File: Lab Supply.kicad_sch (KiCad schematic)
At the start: 38 parts, among them J1 V+, J2 V-, Q1 TIP121, Q2 2N2222, T1 115V to 24V, U1 LM358, U2 LM358

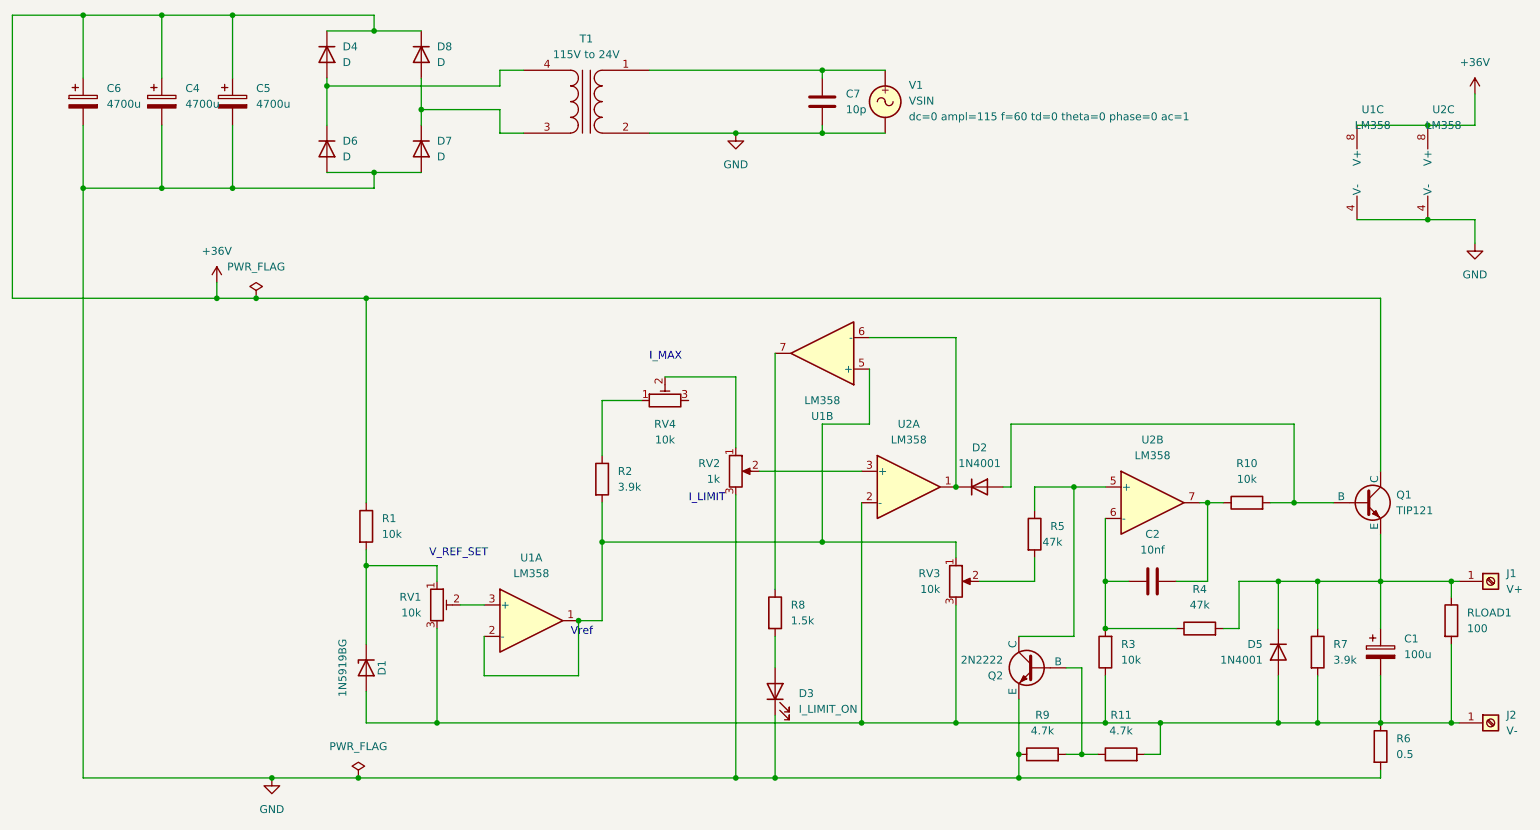
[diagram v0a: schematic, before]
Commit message: Changed to LM324
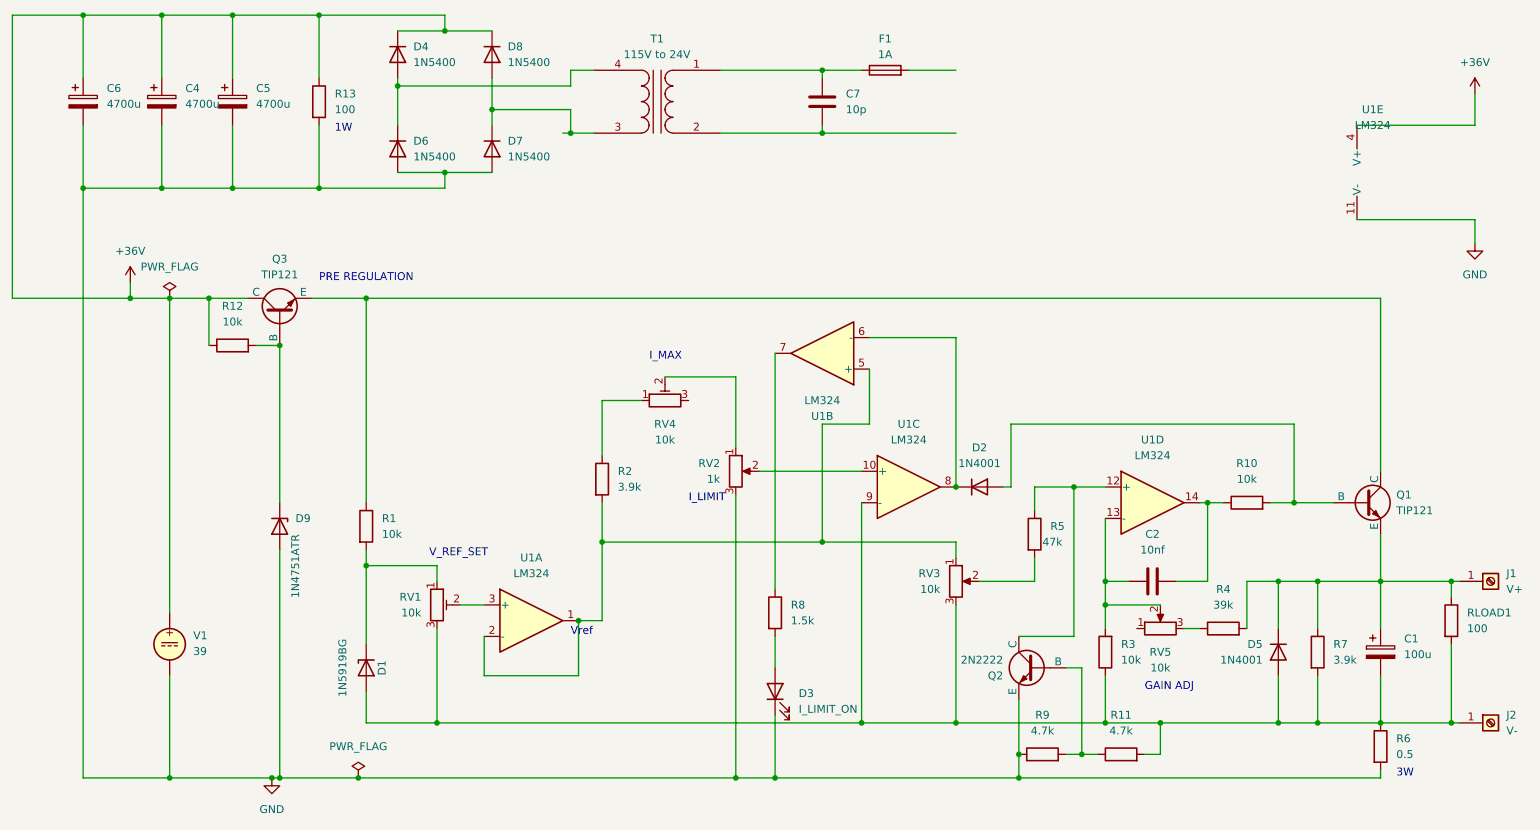
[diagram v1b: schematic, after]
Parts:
- removed unit 3 of U2
- removed V1: VSIN, symbol Simulation_SPICE:VSIN
- added D9: 1N4751ATR, Capacitor_THT:CP_Radial_D8.0mm_P3.50mm, symbol Device:D_Zener
- added F1: 1A, Fuse:Fuseholder_Littelfuse_100_series_5x20mm, symbol Device:Fuse
- added Q3: TIP121, Package_TO_SOT_THT:TO-126-2_Vertical, symbol Simulation_SPICE:NPN
- added R12: 10k, Resistor_THT:R_Axial_DIN0207_L6.3mm_D2.5mm_P2.54mm_Vertical, symbol Device:R
- added R13: 100, Resistor_THT:R_Axial_DIN0207_L6.3mm_D2.5mm_P2.54mm_Vertical, symbol Device:R
- added RV5: 10k, symbol Device:R_Potentiometer
- added V1: 39, symbol Simulation_SPICE:VDC
- C1: footprint (none) -> Capacitor_THT:CP_Radial_D8.0mm_P3.50mm
- C2: footprint Capacitor_THT:CP_Radial_D8.0mm_P3.50mm -> Capacitor_THT:C_Rect_L10.0mm_W2.5mm_P7.50mm_MKS4
- C4, C5, C6: footprint (none) -> Capacitor_THT:CP_Radial_D18.0mm_P7.50mm
- D1: footprint Diode_THT:D_DO-201_P15.24mm_Horizontal -> Diode_THT:D_DO-41_SOD81_P10.16mm_Horizontal
- D4, D6, D7, D8: value D -> 1N5400; footprint (none) -> Diode_THT:D_DO-201AD_P12.70mm_Horizontal
- Q1: footprint Package_TO_SOT_THT:TO-220-2_Vertical -> Package_TO_SOT_THT:TO-220-3_Vertical
- Q2: footprint (none) -> Package_TO_SOT_THT:TO-92_HandSolder
- R1: footprint Resistor_SMD:R_0201_0603Metric -> Resistor_THT:R_Axial_DIN0207_L6.3mm_D2.5mm_P2.54mm_Vertical
- R11, R5, R9: footprint (none) -> Resistor_THT:R_Axial_DIN0207_L6.3mm_D2.5mm_P2.54mm_Vertical
- R4: value 47k -> 39k
- RV1: footprint Potentiometer_THT:Potentiometer_Bourns_PTA6043_Single_Slide -> Potentiometer_THT:Potentiometer_Runtron_RM-065_Vertical
- RV2, RV3: footprint (none) -> Potentiometer_THT:Potentiometer_Alpha_RD901F-40-00D_Single_Vertical
- RV4: footprint (none) -> Potentiometer_THT:Potentiometer_Runtron_RM-065_Vertical
- U1: value LM358 -> LM324; footprint Package_DIP:DIP-8_W7.62mm -> Package_DIP:DIP-16_W7.62mm; symbol Amplifier_Operational:LM358 -> Amplifier_Operational:LM324
- U1: renamed from U2; value LM358 -> LM324; footprint Package_DIP:DIP-8_W7.62mm -> Package_DIP:DIP-16_W7.62mm; symbol Amplifier_Operational:LM358 -> Amplifier_Operational:LM324
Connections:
- net +36V: now also U1.4 (V+), Q3.1 (C), R12.1, R13.1, V1.1; no longer Q1.1 (C), R1.1, U1.8 (V+)
- net GND: now also U1.11 (V-), D9.2 (A), R13.2, V1.2; no longer C7.2, T1.2 (AB), U1.4 (V-)
- net at D2.1 (K), U1.6 (-): now also U1.8; no longer U1.1
- net at C1.2, D1.2 (A), D5.2 (A)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: now also U1.9 (-); no longer U1.2 (-)
- net at C7.1, T1.1 (AA): now also F1.1
- net at Q2.1 (C), R5.1: now also U1.12 (+); no longer U1.5 (+)
- net at C2.1, R3.2: now also U1.13 (-), RV5.2; no longer R4.1, U1.6 (-)
- net at C2.2, R10.1: now also U1.14; no longer U1.7
- net at RV2.2: now also U1.10 (+); no longer U1.3 (+)
- new net: Q1.1 (C), Q3.3 (E), R1.1
- new net: C7.2, T1.2 (AB)
- new net: D9.1 (K), Q3.2 (B), R12.2
- new net: R4.1, RV5.3
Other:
- note added: "1W"
- note added: "3W"
- note added: "GAIN ADJ"
- note added: "PRE REGULATION"
- moved on the sheet: D4, D6, D7, D8, R4, T1

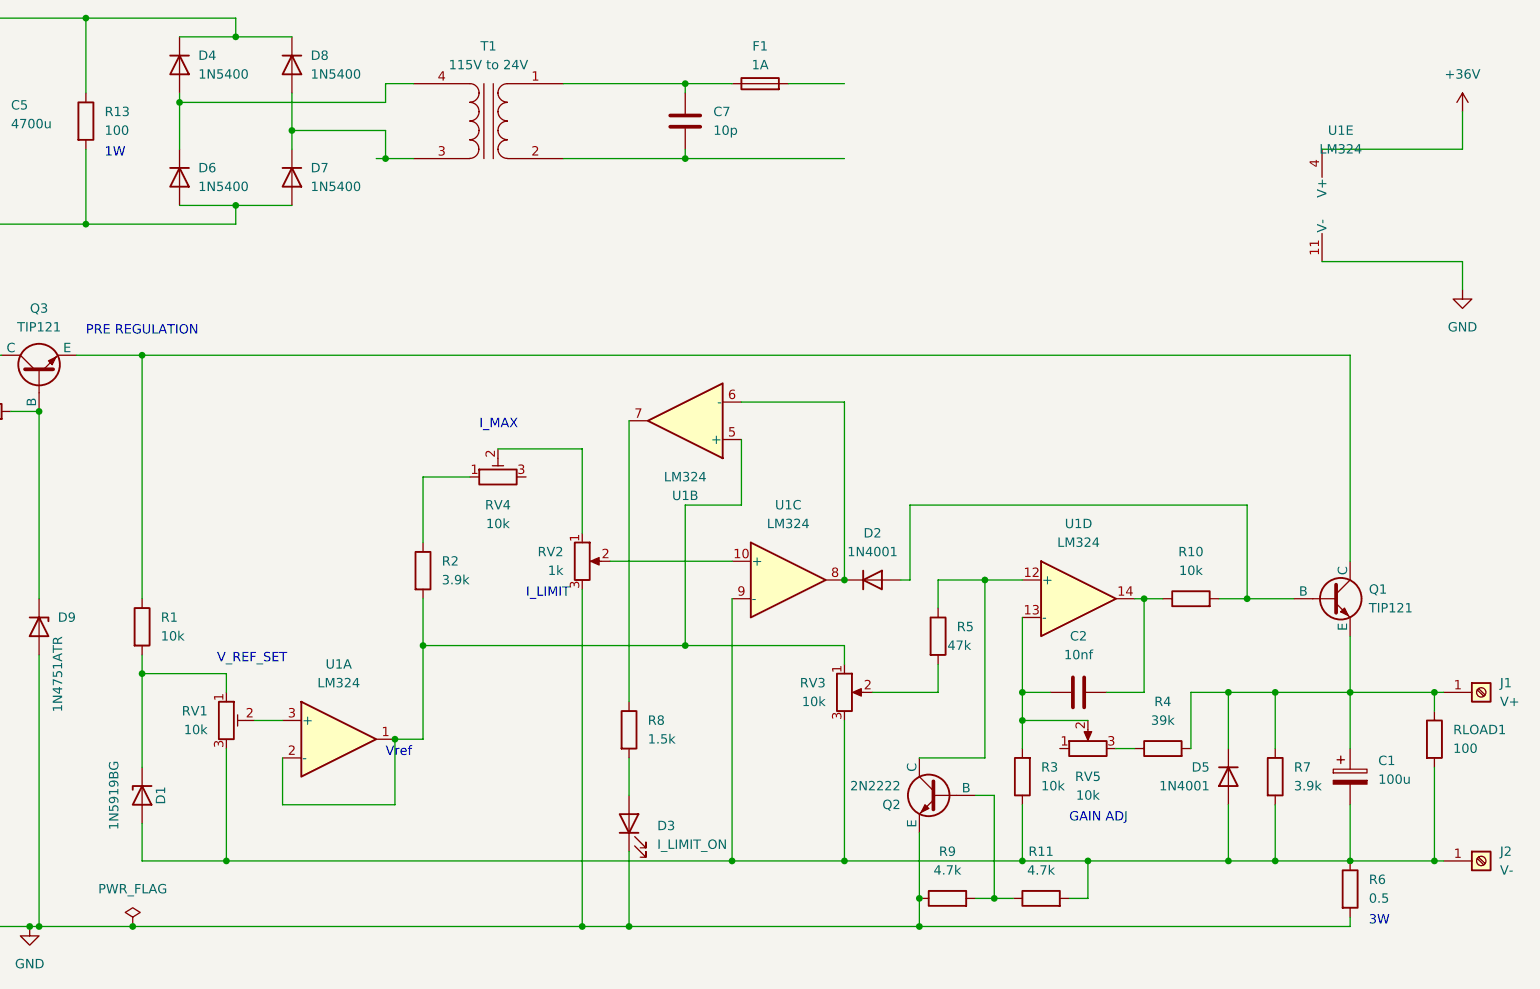
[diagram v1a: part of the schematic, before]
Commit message: Redesigned CC indicator
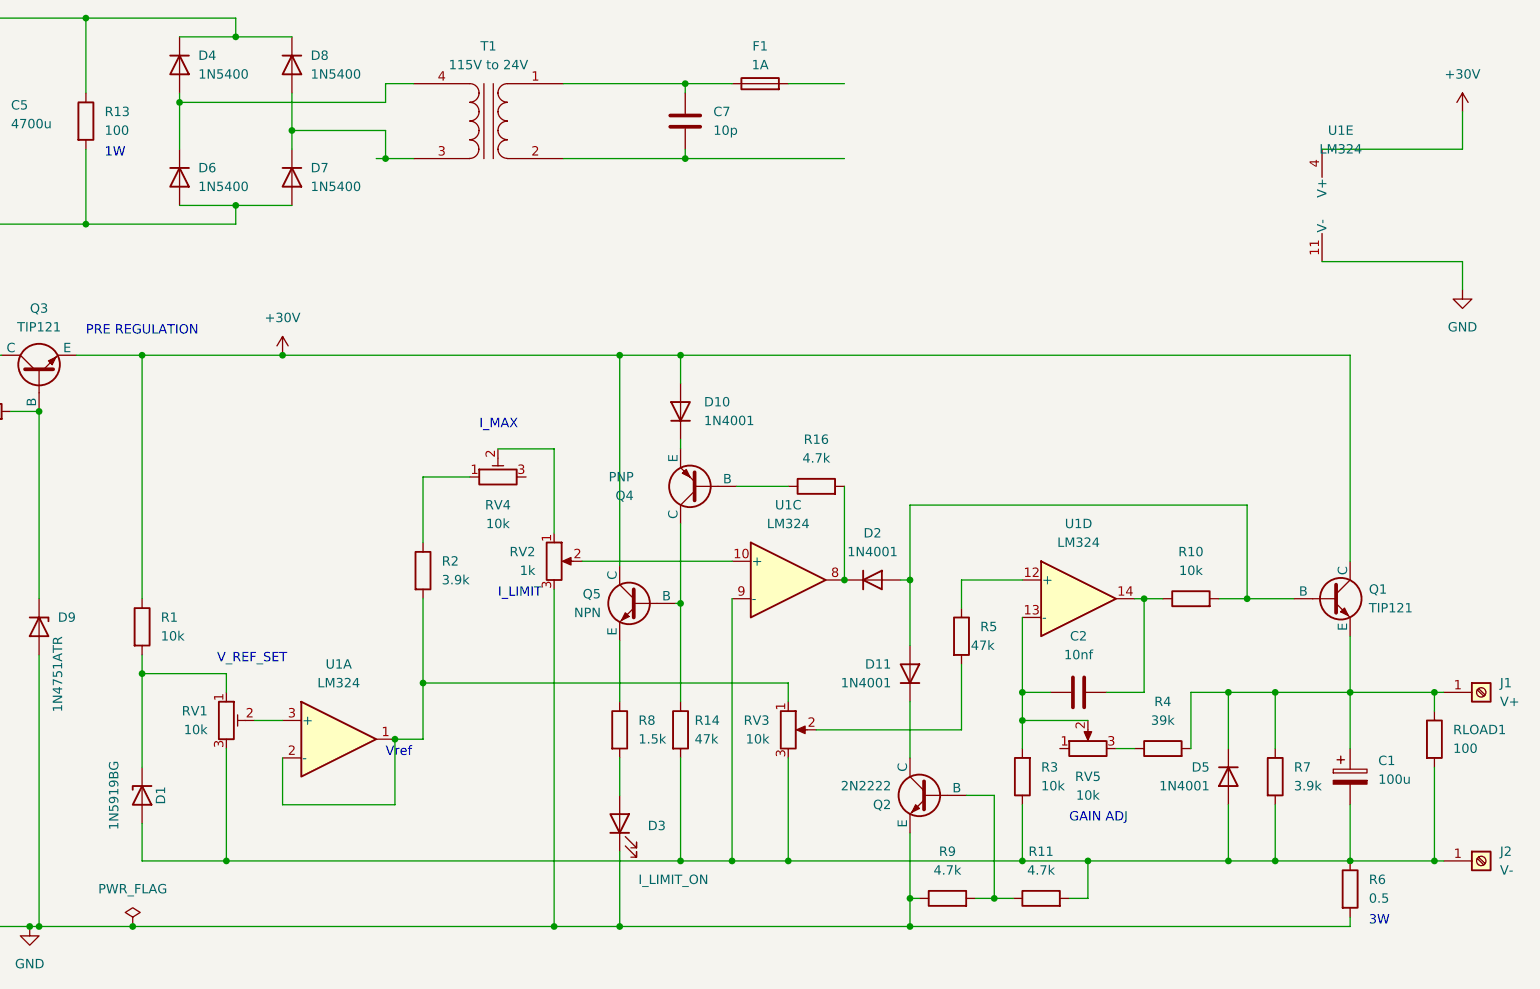
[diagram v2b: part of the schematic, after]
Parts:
- removed unit 2 of U1
- added D10, D11: 1N4001, symbol Device:D
- added Q4: PNP, symbol Simulation_SPICE:PNP
- added Q5: NPN, symbol Simulation_SPICE:NPN
- added R14: 47k, symbol Device:R
- added R16: 4.7k, symbol Device:R
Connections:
- net +36V: no longer U1.4 (V+)
- net at D2.1 (K), U1.8: now also R16.2
- net at D2.2 (A), Q1.2 (B), R10.2: now also D11.2 (A)
- net +28V: now reaches Q1.1 (C), Q3.3 (E), R1.1
- net +28V: now also U1.4 (V+), D10.2 (A), Q5.1 (C)
- net at C1.2, D1.2 (A), D5.2 (A)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: now also R14.2
- net at R5.1, U1.12 (+): no longer Q2.1 (C)
- net at R8.1: now also Q5.3 (E)
- new net: D10.1 (K), Q4.3 (E)
- new net: D11.1 (K), Q2.1 (C)
- new net: Q4.1 (C), Q5.2 (B), R14.1
- new net: Q4.2 (B), R16.1
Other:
- moved on the sheet: D3, Q2, R5, R8, RV2, RV3

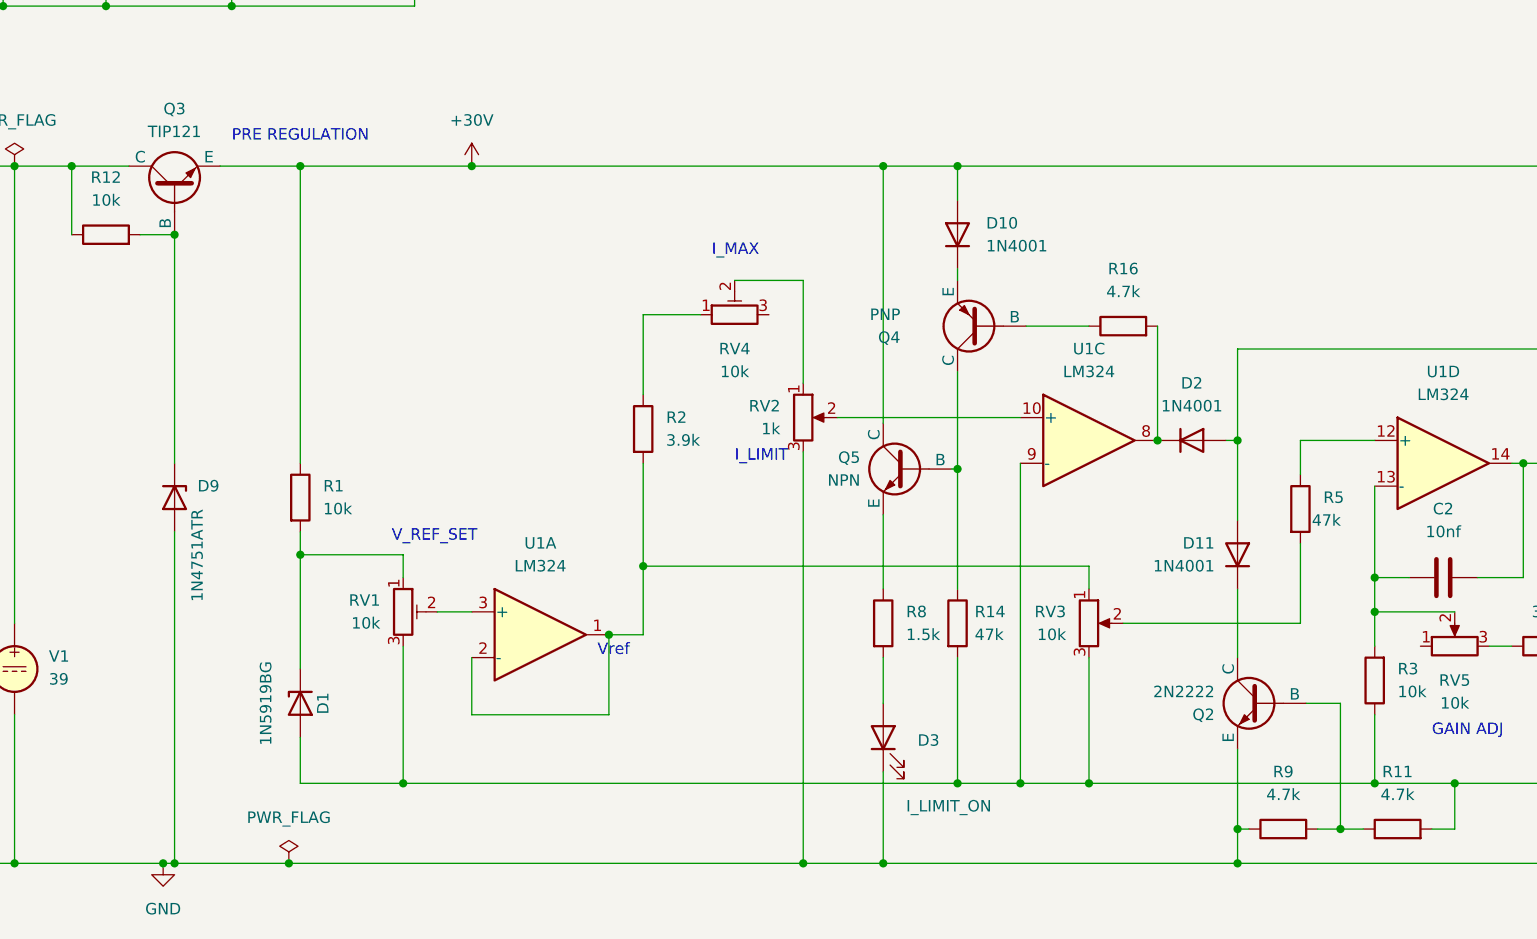
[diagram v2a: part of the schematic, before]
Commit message: Added DA cinverter
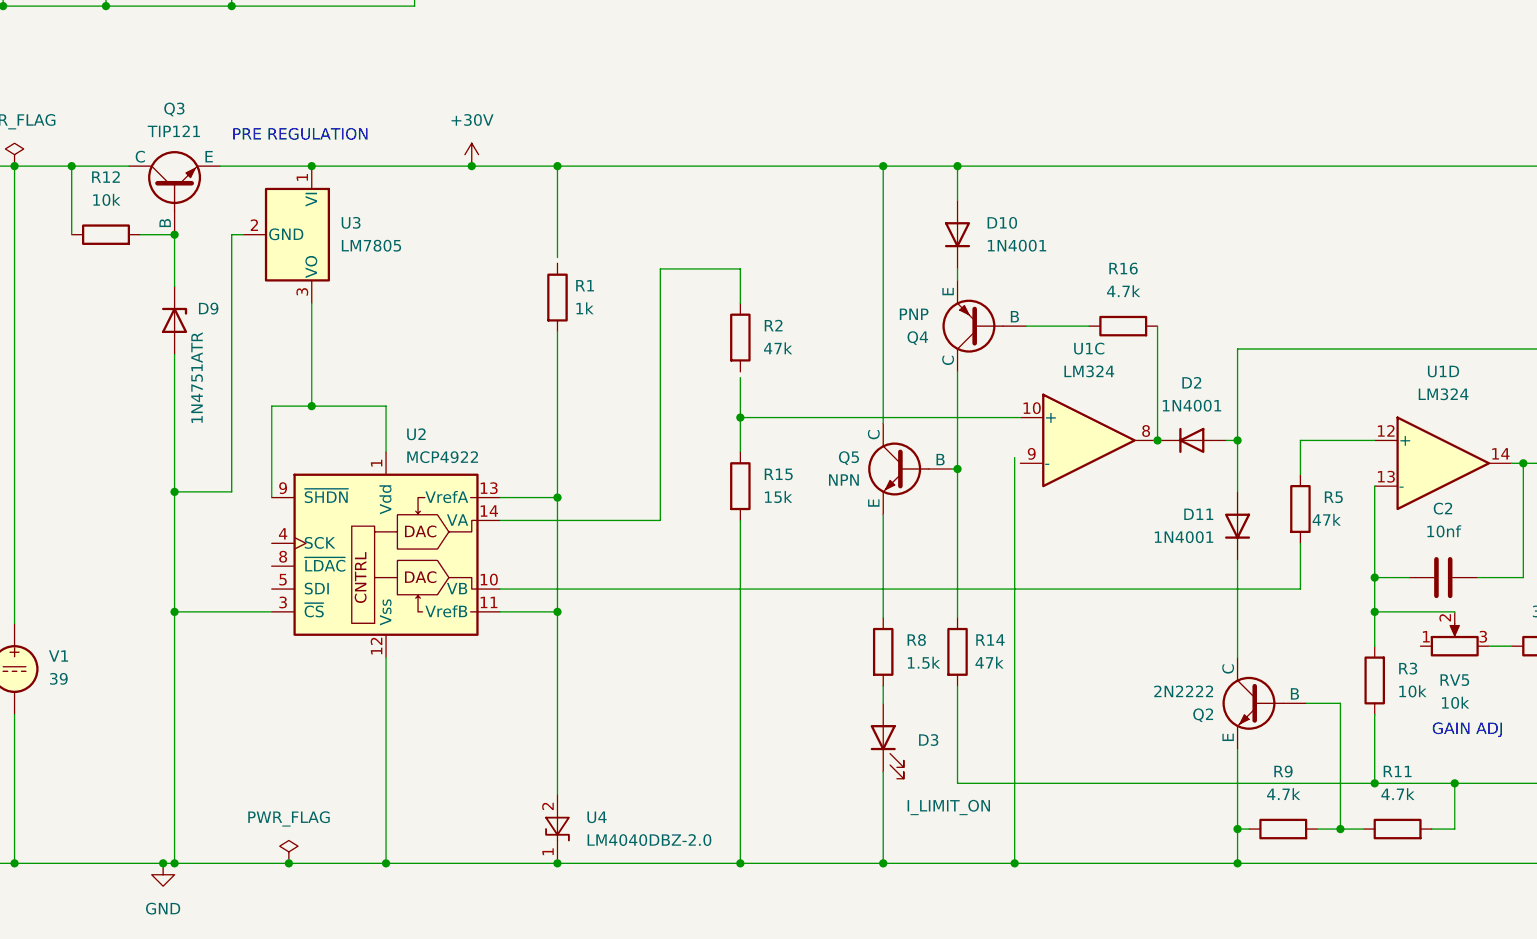
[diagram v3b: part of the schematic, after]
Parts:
- removed D1: 1N5919BG, Diode_THT:D_DO-41_SOD81_P10.16mm_Horizontal, symbol Diode:1N53xxB
- removed RV1, RV4: 10k, Potentiometer_THT:Potentiometer_Runtron_RM-065_Vertical, symbol Device:R_Potentiometer_Trim
- removed RV2: 1k, Potentiometer_THT:Potentiometer_Alpha_RD901F-40-00D_Single_Vertical, symbol Device:R_Potentiometer
- removed RV3: 10k, Potentiometer_THT:Potentiometer_Alpha_RD901F-40-00D_Single_Vertical, symbol Device:R_Potentiometer
- removed unit 1 of U1
- added R15: 15k, symbol Device:R
- added U2: MCP4922, symbol Analog_DAC:MCP4922
- added U3: LM7805, Package_TO_SOT_THT:TO-220-3_Vertical, symbol Regulator_Linear:LM7805_TO220
- added U4: LM4040DBZ-2.0, Package_TO_SOT_SMD:SOT-23, symbol Reference_Voltage:LM4040DBZ-2.0
- R1: value 10k -> 1k; footprint Resistor_THT:R_Axial_DIN0207_L6.3mm_D2.5mm_P2.54mm_Vertical -> (none)
- R2: value 3.9k -> 47k; footprint Resistor_THT:R_Axial_DIN0207_L6.3mm_D2.5mm_P2.54mm_Vertical -> (none)
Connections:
- net +28V: now also U3.1 (VI); no longer R1.1
- net GND: now also R15.2, U2.12 (Vss), U2.3 (~{CS}), U3.2 (GND), U4.1 (K)
- net at C1.2, D5.2 (A), J2.1 (Pin_1)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: no longer U1.9 (-)
- net at R5.2: now also U2.10 (VB)
- net at R2.1: now also U2.14 (VA)
- net at R1.2: now also U2.11 (VrefB), U2.13 (VrefA), U4.2 (A)
- net at U1.10 (+): now also R15.1
- new net: U2.1 (Vdd), U2.9 (~{SHDN}), U3.3 (VO)
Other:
- note removed: "I_LIMIT"
- note removed: "I_MAX"
- note removed: "V_REF_SET"
- note removed: "Vref"
- moved on the sheet: D11, D9, R14, R8
